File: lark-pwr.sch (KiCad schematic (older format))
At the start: 28 parts, among them J4 PWR_IN, U1 AP2112K-3.3, U2 R-785.0-1.0, U3 MCP1700T-3302E_TT, U4 MCP1700T-3302E_TT

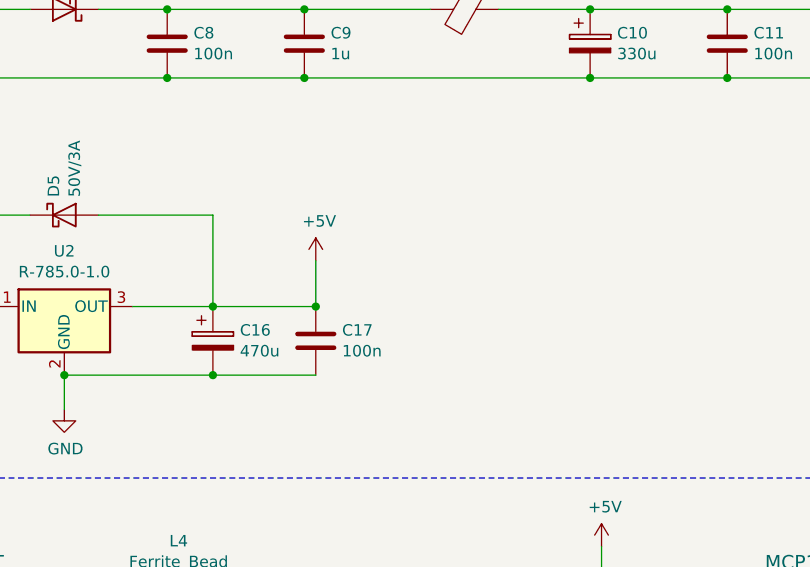
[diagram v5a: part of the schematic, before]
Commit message: Use BMI088 instead of BMX055.
Symbol for BMI088 was created and placed in the schematic.

Still looking for a LGA-16 4.5x3.0 footprint. Do we really need to
create that ourselves?
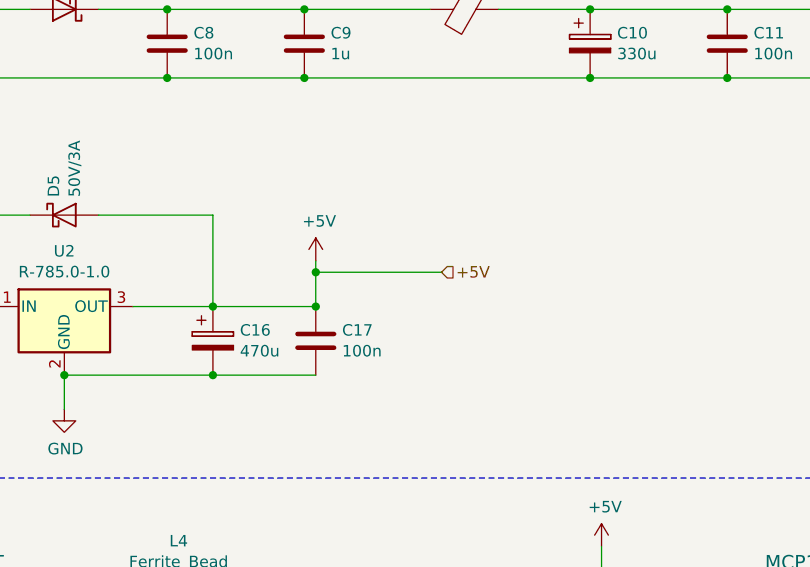
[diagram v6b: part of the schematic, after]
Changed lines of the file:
@@
 $EndComp
 Wire Wire Line
-	3850 2300 3850 2100
+	3850 2300 3850 2150
 Connection ~ 2750 2600
 Wire Wire Line
@@
 Text HLabel 2100 2300 0    50   Input ~ 0
 PWRIN
+Wire Wire Line
+	3850 2150 4400 2150
+Connection ~ 3850 2150
+Wire Wire Line
+	3850 2150 3850 2100
+Text HLabel 4400 2150 2    50   Input ~ 0
++5V
 $EndSCHEMATC

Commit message: Fitting layout into 57 mm instrument.
* board width is 51 mm at the moment
* split into two boards (sensor and main) which can be stacked with
  2.54 mm pinheaders.
* ESP32 was put to bottom with optional pcb antenna facing to front.
* added footprint for optional HCLAxxE on sensorboard
* added footprint for BMI088

* Is multiple GND pins for sensor board really a good idea (ground loops)?
* Does the +12V topology make sense (especially regarding the external
  IGC ports)?
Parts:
- removed C21, C22, C23: 1u, Capacitor_SMD:C_0805_2012Metric_Pad1.15x1.40mm_HandSolder, symbol lark-rescue:C-Device
- removed D3: 50V/3A, Diode_SMD:D_SOD-123, symbol lark-rescue:D_Schottky-Device
- removed L1: 6A max., Inductor_SMD:L_1206_3216Metric_Pad1.42x1.75mm_HandSolder, symbol lark-rescue:Ferrite_Bead-Device
- removed L4: Ferrite_Bead, Inductor_SMD:L_0805_2012Metric_Pad1.15x1.40mm_HandSolder, symbol lark-rescue:Ferrite_Bead-Device
- removed U4: MCP1700T-3302E_TT, Package_TO_SOT_SMD:SOT-23, symbol lark-rescue:MCP1700T-3302E_TT-dk_PMIC-Voltage-Regulators-Linear
- added L1: 10uH, Inductor_SMD:L_Wuerth_WE-PD2-Typ-L, symbol Device:L
- C12, C9: value 1u -> 10u
- D4, D5: footprint Diode_SMD:D_SOD-123 -> Diode_SMD:D_SMA_Handsoldering
- F1: renamed from RV1; footprint Fuse:Fuse_2920_7451Metric_Pad2.10x5.45mm_HandSolder -> Fuse:Fuse_1812_4532Metric_Pad1.30x3.40mm_HandSolder; symbol lark-rescue:Varistor-Device -> Device:Polyfuse
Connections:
- net +12V: now also C8.1, C9.1, D4.1 (K), F1.1, L1.1; no longer C11.1, C12.1, D5.1 (K), U2.1 (IN)
- new net PWRIN: C11.1, C12.1, D5.1 (K), L1.2, U2.1 (IN)
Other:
- moved on the sheet: C10, C11, C12
